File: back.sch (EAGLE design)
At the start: 34 parts, among them IC2 74AHC1G125DBV, IC3 74AHC1G125DBV, M1 HX1, X1 BU-SMA-V

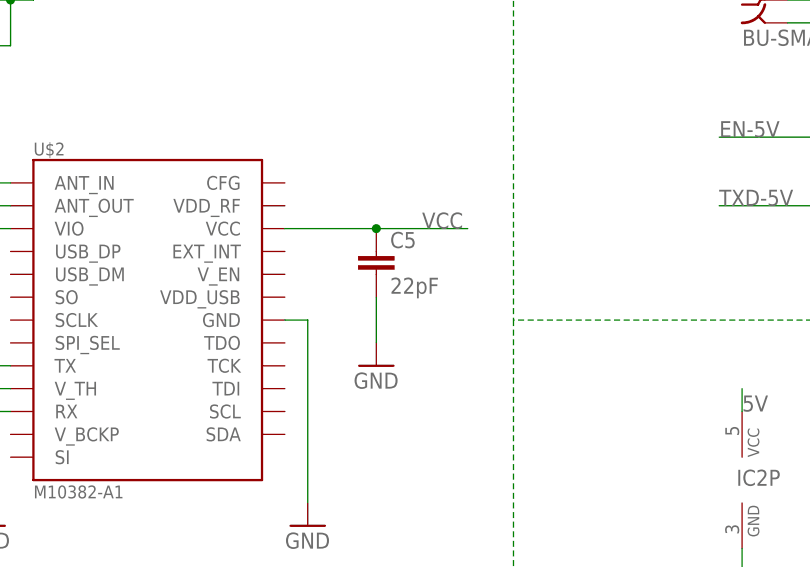
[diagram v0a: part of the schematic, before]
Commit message: Starting Board Work (caps near component they're for)
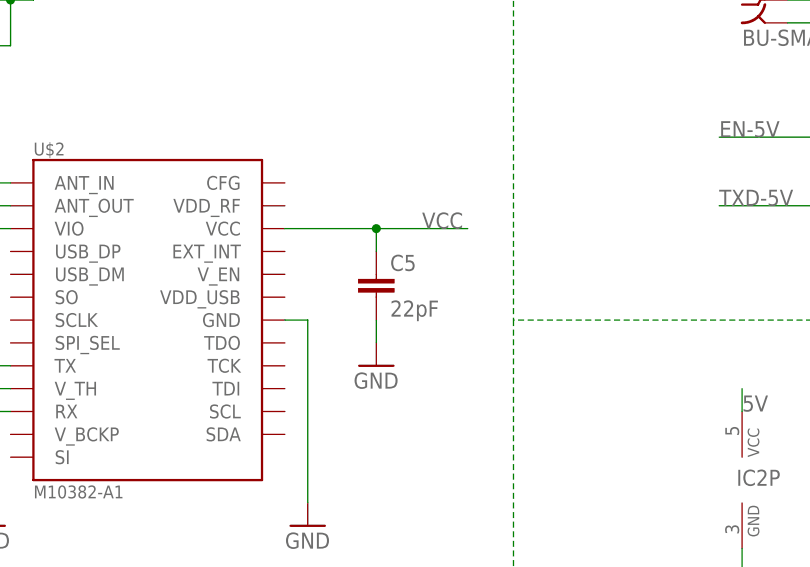
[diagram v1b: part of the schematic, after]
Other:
- moved on the sheet: C5
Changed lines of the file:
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@@
 <instance part="C2" gate="G$1" x="-175.26" y="147.32"/>
 <instance part="C3" gate="G$1" x="-180.34" y="175.26"/>
-<instance part="C5" gate="G$1" x="-93.98" y="170.18"/>
+<instance part="C5" gate="G$1" x="-93.98" y="167.64"/>
 <instance part="C6" gate="G$1" x="-139.7" y="200.66" rot="R90"/>
 <instance part="GND1" gate="1" x="-175.26" y="137.16"/>
@@
 <pinref part="C5" gate="G$1" pin="1"/>
 <wire x1="-93.98" y1="175.26" x2="-83.82" y2="175.26" width="0.1524" layer="91"/>
+<wire x1="-93.98" y1="175.26" x2="-93.98" y2="172.72" width="0.1524" layer="91"/>
 <junction x="-93.98" y="175.26"/>
 <label x="-88.9" y="175.26" size="1.778" layer="95"/>
@@
 <segment>
 <pinref part="C5" gate="G$1" pin="2"/>
-<wire x1="-93.98" y1="167.64" x2="-93.98" y2="162.56" width="0.1524" layer="91"/>
+<wire x1="-93.98" y1="165.1" x2="-93.98" y2="162.56" width="0.1524" layer="91"/>
 <pinref part="GND8" gate="1" pin="GND"/>
 </segment>
